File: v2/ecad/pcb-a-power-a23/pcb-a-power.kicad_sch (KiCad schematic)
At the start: 428 parts, among them Q1 2N7002: panel controller high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, Q10 CSD18510Q5B 40 V N-FET, Q11 CSD18510Q5B 40 V N-FET, Q12 CSD18510Q5B 40 V N-FET, Q13 CSD18510Q5B 40 V N-FET, Q14 CSD18510Q5B 40 V N-FET, Q15 CSD18510Q5B 40 V N-FET, Q16 CSD18510Q5B 40 V N-FET, Q17 CSD19532Q5B 100 V N-FET (4.6 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, Q18 CSD19532Q5B 100 V N-FET (4.6 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, Q19 CSD19532Q5B 100 V N-FET (4.6 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, Q2 CSD19532Q5B 100 V N-FET (4.6 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, Q20 CSD19532Q5B 100 V N-FET (4.6 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, Q21 CSD18510Q5B 40 V N-FET, Q22 CSD18510Q5B 40 V N-FET, Q23 CSD18510Q5B 40 V N-FET, Q24 CSD18510Q5B 40 V N-FET, Q25 CSD18510Q5B 40 V N-FET, Q26 CSD18510Q5B 40 V N-FET, Q27 CSD18510Q5B 40 V N-FET (VBUS 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, Q3 CSD19532Q5B 100 V N-FET (4.6 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, Q4 CSD19532Q5B 100 V N-FET (4.6 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, Q5 CSD19532Q5B 100 V N-FET (4.6 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, Q6 2N7002: CHG_INHIBIT high = IL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, Q7 CSD18510Q5B 40 V N-FET, Q8 CSD18510Q5B 40 V N-FET, Q9 CSD18510Q5B 40 V N-FET, U1 LTC2954CTS8-1 push-button on/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, U10 INA226 rail monitor +5V_S3, U11 INA226 rail monitor +5V_DEV, U12 TPS62933DRLR 3 A buck, 3.3 V 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, U13 LM5176PWPR buck-boost control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, U14 INA226 PA rail monitor (0x46), U15 LM5176PWPR buck-boost control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, U16 LM5176PWPR buck-boost control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, U17 INA226 PoE rail monitor (0x47), U18 TPS25740ARGER USB-C PD source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, U19 LM5176PWPR buck-boost control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, U2 LM5176PWPR buck-boost control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, U21 TPS259631DDAR eFuse VBAT -> V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, U22 TPS259631DDAR eFuse VBAT -> V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, U23 TPS259631DDAR eFuse +5V_DEV -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, U26 SN74LVC08APWR quad AND: EMCON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, U27 PCA9555PW (0x21): enables and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, U28 PCA9555PW (0x24): power-good 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, U29 USBLC6-2SC6, U3 BQ25731RSNR 1 to 5 cell buck-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, U4 AP64500SP-13 5 A buck, 5.1 V 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, U5 AP64500SP-13 5 A buck, 5.1 V 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, U6 AP64500SP-13 5 A buck, 5.1 V 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, U7 AP64500SP-13 5 A buck, 5.1 V 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, U8 INA226 rail monitor +5V_S1, U9 INA226 rail monitor +5V_S2

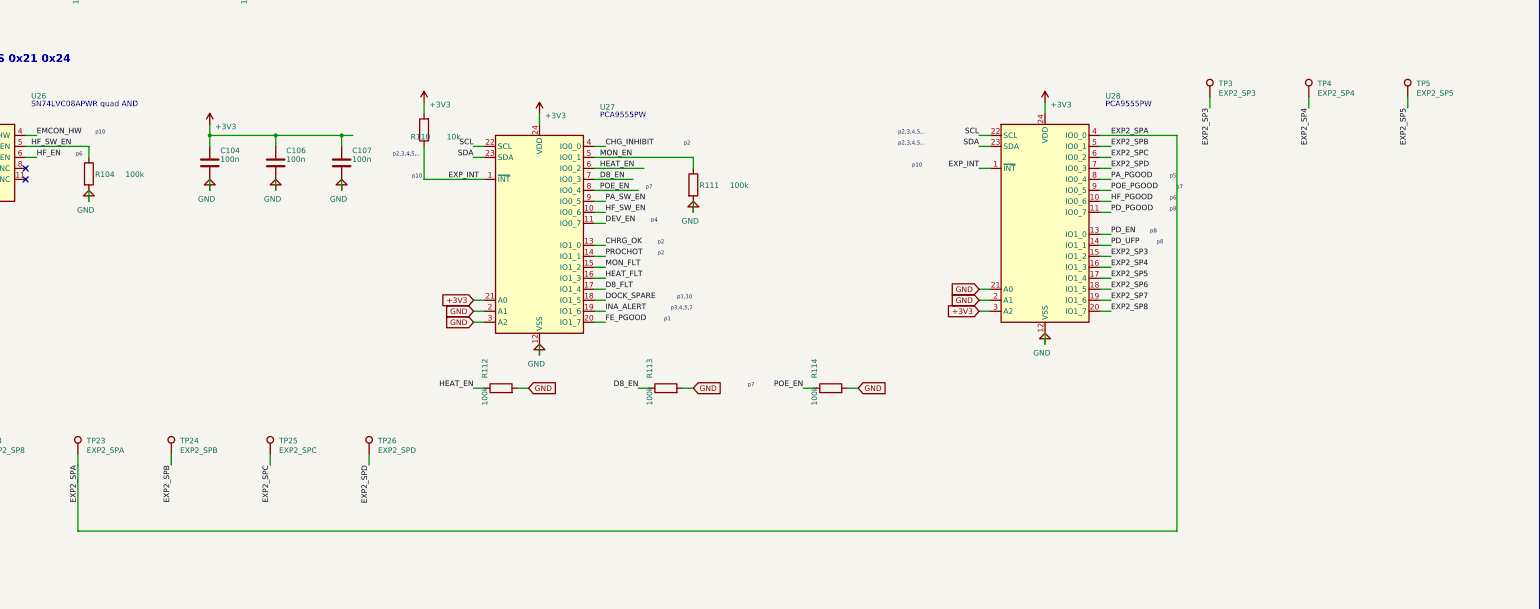
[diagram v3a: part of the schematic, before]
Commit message: fix(pcb-a): four decoupling capacitors were in a region at the other end of the board [MESHSAT-709]
C4, C104, C106 and C107 are named in region CTL at case x 52 to 90 while U1, U26, U27 and U28 are fixed at x -49 to -62, so each sat 109.4, 139.6, 114.6 and 130.7 mm from the pin it decouples. Seats measured on A70's placed board put all four within 1.70 to 1.90 mm with nothing else moved, and the chain proves them at hard 0 with 461 escapes and 2 pads skipped, both the baseline's.

The first arm improved five rows to seven instead of nine, which found the second defect: C106 and C107 are the two expanders' own decoupling and both were declared against U26 pin 14, a part neither serves. With both corrections the chain at HEAD reads 0 moved, 9 already within 3.0 mm, 31 stuck of 40, RESULT ALL PASS and netlist_board 2,148 of 2,148.

The generator edit owes a regeneration: board A's schematic, netlist, sidecar and intent are rebuilt at its own phase and move in this commit. The netlist is identical connection for connection, differing only in its source line, its date and KiCad's own tstamps.
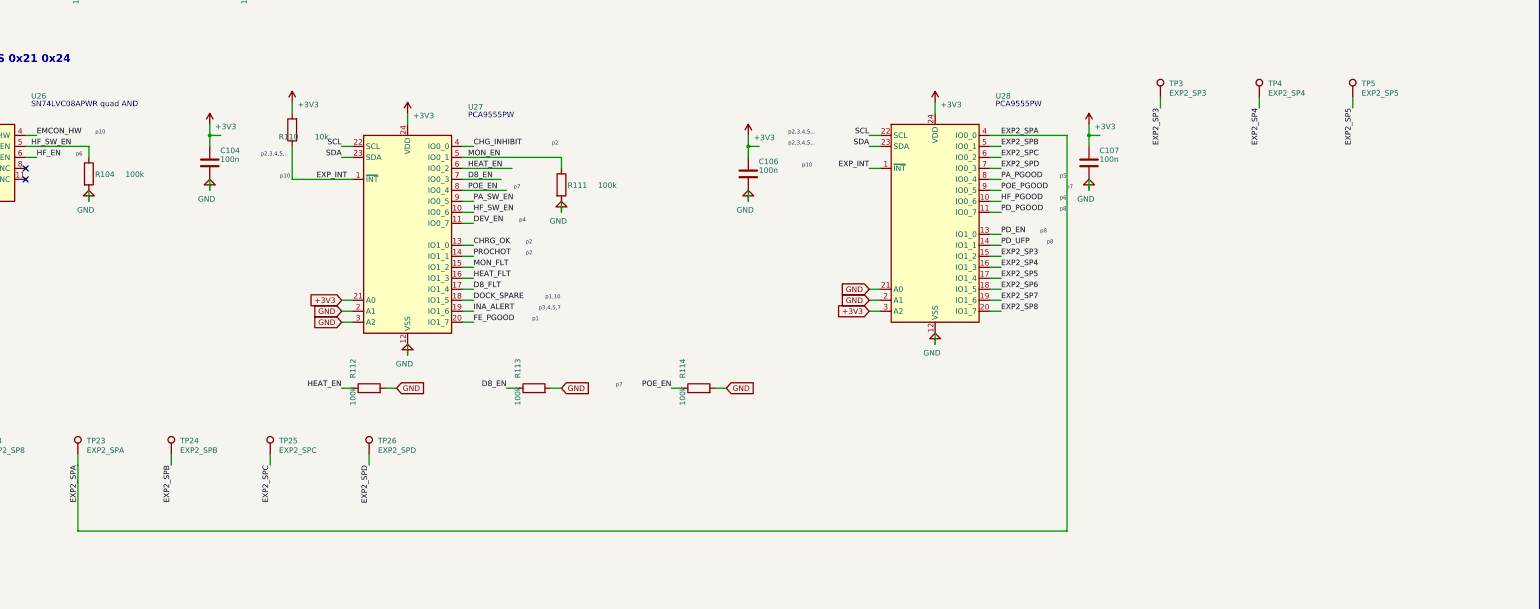
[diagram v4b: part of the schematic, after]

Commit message: fix(v2): boards A, B and D take their round-4 and round-6 circuit corrections, regenerated with parity and every difference traced [MESHSAT-1357]
Review D (parts and circuits) for boards A, B and D. Each board was approved by its reviewer with no blocking item left. This is a prototype design: nothing here has been built or measured, and this commit does not place, route, promote or order any board. Every choice that had more than one option was taken by the session under the owner's standing rule of 26 Sep 2026.

Board A, power and I/O:
- The charger's cell strap now reads 4S (R26 13.3k). The kit sits on the charger's VSYS: the pack reaches VBAT through the blade F1 and the RSR shunt R17 (S-03, S-04).
- Slot rail 2 and the device rail are LM5176 stages with a 7.2 A minimum average limit. The PA rail is limited by its stage's own average current loop (F-PR-04, F-PR-01).
- The heater mat runs from a regulated 12 V buck, U33 (F-PR-06).
- Every LM5176 stage has bootstrap diodes, a slope capacitor, its own loop design and BIAS from VBAT with a bypass. VIN blocking diodes sit on the three stages with external BIAS (R4A-N1, R4A-N2, B2, R4A-N6, R4A-N11).
- The front end has VBUS20 bulk sized for its ripple current, a 4.7 uF soft start sized for board E's vehicle entry, and VISNS behind 2k. A restart guard, U34 (TPS37A010122), holds U2 off until VBUS20 is bled (B3, B4, R4A-N15).
- Power-up: industrial-grade LTC2954, KILL on +3V3, a defined RAIL_EN, PDT set for a four-second override, and resized PI_KILL and PI_SHDN_REQ pulls (S-08).
- A NAND interlock drops the PoE and PD outlets while the PA keys (S-14).
- A low-capacitance ESD array sits on the USB-C CC pins (D-17). The wall data path goes to the Glenair port behind its own eFuse, U32, and the USB-C outlet becomes power only (D-12).

Board B, compute:
- PCIe lanes run from each transmitter to its receiver, with series coupling at the switch. The LimeSDR SuperSpeed pairs run transmitter to receiver. Every used REFCLKO pair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
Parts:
- removed C38, C56: 22u 10V X7R 1210, Capacitor_SMD:C_1210_3225Metric, symbol Device:C
- removed C65, C92: 10u 50V X7R 1210, Capacitor_SMD:C_1210_3225Metric, symbol Device:C
- removed C7: 47n, Capacitor_SMD:C_0603_1608Metric, symbol Device:C
- removed J_PA: 13.8 V to the PA module on the face plate (JST-VH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, Connector_JST:JST_VH_B2P-VH_1x02_P3.96mm_Vertical, symbol Connector_Generic:Conn_01x02
- removed L7: 4.7uH XAL4030-472ME, Inductor_SMD:L_Coilcraft_XAL4030-XXX, symbol Device:L
- removed L8: 6.8uH XAL1010-682ME (Isat 17 A), Inductor_SMD:L_Coilcraft_XAL1010-XXX, symbol Device:L
- removed Q2: CSD19532Q5B 100 V N-FET (4.6 mOhm at VGS 6 V, Pow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, Package_SO:PowerPAK_SO-8_Single, symbol meshsat_ic:Q2
- removed Q23: CSD18510Q5B 40 V N-FET, Package_SO:PowerPAK_SO-8_Single, symbol meshsat_ic:Q23
- removed Q25: CSD18510Q5B 40 V N-FET, Package_SO:PowerPAK_SO-8_Single, symbol meshsat_ic:Q25
- removed R10: 10k, Resistor_SMD:R_0603_1608Metric, symbol Device:R
- removed R31: 5mOhm 1% 2512 (shunt), Resistor_SMD:R_2512_6332Metric, symbol Device:R
- removed R46: 68k (RT: 500 kHz), Resistor_SMD:R_0603_1608Metric, symbol Device:R
- removed R52: 40.2k (300 kHz), Resistor_SMD:R_0603_1608Metric, symbol Device:R
- removed R53, R63, R69, R79, R9: 30k (slope), Resistor_SMD:R_0603_1608Metric, symbol Device:R
- removed R60: 140k 1%, Resistor_SMD:R_0603_1608Metric, symbol Device:R
- removed R72: 10mOhm 1% 2512 (CS), Resistor_SMD:R_2512_6332Metric, symbol Device:R
- removed R90: 750R 1% (ILM: 1.2 A), Resistor_SMD:R_0603_1608Metric, symbol Device:R
- removed U8: INA226 rail monitor +5V_S1, Package_SO:VSSOP-10_3x3mm_P0.5mm, symbol meshsat_ic:U8
- added C10, C137, C144, C46, C9: 100n 25V, Capacitor_SMD:C_0603_1608Metric, symbol Device:C
- added C112: 3.3n, Capacitor_SMD:C_0603_1608Metric, symbol Device:C
- added C129, C130, C134, C138, C141, C145, C146, C191: 1n, Capacitor_SMD:C_0603_1608Metric, symbol Device:C
- added C133, C140, C148, C149, C151: 470p, Capacitor_SMD:C_0603_1608Metric, symbol Device:C
- added C135, C142: 47n, Capacitor_SMD:C_0603_1608Metric, symbol Device:C
- added C136, C143: 4.7u, Capacitor_SMD:C_0805_2012Metric, symbol Device:C
- added C150: 560p, Capacitor_SMD:C_0603_1608Metric, symbol Device:C
- added C152: 680n, Capacitor_SMD:C_0603_1608Metric, symbol Device:C
- added C153, C155, C157, C160, C192, C193, C194, C195, C196, C197, C198, C212, C214, C52: 100n, Capacitor_SMD:C_0603_1608Metric, symbol Device:C
- added C154, C158, C190, C211: 10n, Capacitor_SMD:C_0603_1608Metric, symbol Device:C
- added C156, C161, C162, C51: 22u 25V 1210, Capacitor_SMD:C_1210_3225Metric, symbol Device:C
- added C159: 10u 25V 1210, Capacitor_SMD:C_1210_3225Metric, symbol Device:C
- added C163, C178, C179, C180, C199, C200: 330u 35V Panasonic EEHZK1V331P hybrid polymer (10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, Capacitor_SMD:CP_Elec_10x10, symbol Device:C_Polarized
- added C164, C165, C166, C167, C168, C169, C172, C173: 150u 25V Panasonic EEHZK1E151XP hybrid polymer (7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, Capacitor_SMD:CP_Elec_6.3x7.7, symbol Device:C_Polarized
- added C170, C171, C174, C175: 470u 25V Panasonic EEHZK1E471P hybrid polymer (10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, Capacitor_SMD:CP_Elec_10x10, symbol Device:C_Polarized
- added C176, C177: 10u 100V X7R 1210, Capacitor_SMD:C_1210_3225Metric, symbol Device:C
- added C181, C182, C183, C184, C185, C186, C187, C188, C189, C201, C202, C203, C204, C205, C206: 10u 50V X7R 1210, Capacitor_SMD:C_1210_3225Metric, symbol Device:C
- added C207, C210: 1u 100V 1210, Capacitor_SMD:C_1210_3225Metric, symbol Device:C
- added C208, C209: 1u, Capacitor_SMD:C_0603_1608Metric, symbol Device:C
- added C213: 2.2n, Capacitor_SMD:C_0603_1608Metric, symbol Device:C
- added C87: 1.5n, Capacitor_SMD:C_0603_1608Metric, symbol Device:C
- added D10, D11, D12, D13, D14, D15, D16, D17, D18, D5, D6, D7, D8, D9: BAT46W-7-F Schottky 100V (bootstrap), Diode_SMD:D_SOD-123, symbol Device:D_Schottky
- added D19, D20, D21: BAT46W-7-F Schottky 100V (VIN blocking), Diode_SMD:D_SOD-123, symbol Device:D_Schottky
- added D22: BZT52C12-7-F zener, the restart guard's pull-up c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, Diode_SMD:D_SOD-123, symbol Device:D_Zener
- added D3: SMBJ5.0A, Diode_SMD:D_SMB, symbol Device:D_TVS
- added J_BM9: SMP-MAX slide-on receptacle R222M00720 (underside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, meshsat:Radiall_SMPMAX_R222M00720, symbol Connector:Conn_Coaxial
- added L1: 10uH XAL1010-103ME (Isat 17.5 A), Inductor_SMD:L_Coilcraft_XAL1010-XXX, symbol Device:L
- added L12: 15uH XAL4040-153ME (Isat 2.9 A), Inductor_SMD:L_Coilcraft_XAL4040-XXX, symbol Device:L
- added Q27: CSD18510Q5B 40 V N-FET (VBUS switch), Package_SO:PowerPAK_SO-8_Single, symbol meshsat_ic:Q27
- added Q28: CSD19532Q5B 100 V N-FET (4.6 mOhm at VGS 6 V, Pow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, Package_SO:PowerPAK_SO-8_Single, symbol meshsat_ic:Q28
- added Q29: CSD19532Q5B 100 V N-FET (4.6 mOhm at VGS 6 V, Pow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, Package_SO:PowerPAK_SO-8_Single, symbol meshsat_ic:Q29
- added Q30: CSD19532Q5B 100 V N-FET (4.6 mOhm at VGS 6 V, Pow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, Package_SO:PowerPAK_SO-8_Single, symbol meshsat_ic:Q30
- added Q31: CSD19532Q5B 100 V N-FET (4.6 mOhm at VGS 6 V, Pow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, Package_SO:PowerPAK_SO-8_Single, symbol meshsat_ic:Q31
- added Q32: CSD19532Q5B 100 V N-FET (4.6 mOhm at VGS 6 V, Pow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, Package_SO:PowerPAK_SO-8_Single, symbol meshsat_ic:Q32
- added Q33: CSD19532Q5B 100 V N-FET (4.6 mOhm at VGS 6 V, Pow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, Package_SO:PowerPAK_SO-8_Single, symbol meshsat_ic:Q33
- added Q34: CSD19532Q5B 100 V N-FET (4.6 mOhm at VGS 6 V, Pow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, Package_SO:PowerPAK_SO-8_Single, symbol meshsat_ic:Q34
- added Q35: CSD19532Q5B 100 V N-FET (4.6 mOhm at VGS 6 V, Pow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, Package_SO:PowerPAK_SO-8_Single, symbol meshsat_ic:Q35
- added Q36: 2N7002: FE_RUN high = latch sense held at 0 V (1 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, Package_TO_SOT_SMD:SOT-23, symbol Transistor_FET:2N7002
- added Q37: 2N7002: FE_RUN high = bleed off (1 G, 2 S, 3 D), Package_TO_SOT_SMD:SOT-23, symbol Transistor_FET:2N7002
- added R124: 62k 1%, Resistor_SMD:R_0603_1608Metric, symbol Device:R
- added R135, R172, R179: 100k (MODE: CCM), Resistor_SMD:R_0603_1608Metric, symbol Device:R
- added R142, R187: 10k, Resistor_SMD:R_0603_1608Metric, symbol Device:R
- added R170, R177: 5mOhm 1% 2512 (CS), Resistor_SMD:R_2512_6332Metric, symbol Device:R
- added R173, R180: 100R 1% (CS filter, Kelvin from the shunt's top), Resistor_SMD:R_0603_1608Metric, symbol Device:R
- added R174, R181: 100R 1% (CSG filter, Kelvin from the shunt's grou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, Resistor_SMD:R_0603_1608Metric, symbol Device:R
- added R175, R182: 100R 1% (ISNS+ filter, Kelvin from the shunt's ou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, Resistor_SMD:R_0603_1608Metric, symbol Device:R
- added R176, R183: 100R 1% (ISNS- filter, Kelvin from the shunt's ra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, Resistor_SMD:R_0603_1608Metric, symbol Device:R
- added R178, R193, R197, R198, R201, R206, R4: 100k, Resistor_SMD:R_0603_1608Metric, symbol Device:R
- added R186: 1k 1% (ILM: 0.89 A), Resistor_SMD:R_0603_1608Metric, symbol Device:R
- added R188: 40.2k 1%, Resistor_SMD:R_0603_1608Metric, symbol Device:R
- added R189: 10k 1% (OVLO), Resistor_SMD:R_0603_1608Metric, symbol Device:R
- added R19: 16.5k 1%, Resistor_SMD:R_0603_1608Metric, symbol Device:R
- added R190: 4.7k, Resistor_SMD:R_0603_1608Metric, symbol Device:R
- added R191: 140k 1%, Resistor_SMD:R_0603_1608Metric, symbol Device:R
- added R192: 10k 1%, Resistor_SMD:R_0603_1608Metric, symbol Device:R
- added R194: 20k 1%, Resistor_SMD:R_0603_1608Metric, symbol Device:R
- added R196: 1k, Resistor_SMD:R_0603_1608Metric, symbol Device:R
- added R199: 47k, Resistor_SMD:R_0603_1608Metric, symbol Device:R
- added R200: 33k, Resistor_SMD:R_0603_1608Metric, symbol Device:R
- added R202, R203: 510R 1W 2512 (VBUS20 bleed), Resistor_SMD:R_2512_6332Metric, symbol Device:R
- added R40: 53.6k 1%, Resistor_SMD:R_0603_1608Metric, symbol Device:R
- added R45: 68k (RT: 500 kHz), Resistor_SMD:R_0603_1608Metric, symbol Device:R
- added R6: 240k 1%, Resistor_SMD:R_0603_1608Metric, symbol Device:R
- added R96: 143k 1%, Resistor_SMD:R_0603_1608Metric, symbol Device:R
- added TP21: DOCK_SPARE, TestPoint:TestPoint_Pad_D1.5mm, symbol Connector:TestPoint
- added TP3: EXP2_SP3, TestPoint:TestPoint_Pad_D1.5mm, symbol Connector:TestPoint
- added TP6: EXP2_SP6, TestPoint:TestPoint_Pad_D1.5mm, symbol Connector:TestPoint
- added U12: TPS62933DRLR 3 A buck, 3.3 V logic, Package_TO_SOT_SMD:SOT-583-8, symbol meshsat_ic:U12
- added U17: INA226 PoE rail monitor (0x47), Package_SO:VSSOP-10_3x3mm_P0.5mm, symbol meshsat_ic:U17
- added U19: LM5176PWPR buck-boost controller, PD_VPWR from VB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, Package_SO:HTSSOP-28-1EP_4.4x9.7mm_P0.65mm_EP2.85x5.4mm, symbol meshsat_ic:U19
- added U30: SN74LVC1G00DBVR NAND: OUTLET_OK = NOT (TR_APRS AN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, Package_TO_SOT_SMD:SOT-23-5, symbol meshsat_ic:U30
- added U32: TPS259631DDAR eFuse +5V_DEV -> VBUS_WALL (1k 1% (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, Package_SO:SOIC-8-1EP_3.9x4.9mm_P1.27mm_EP2.29x3mm, symbol meshsat_ic:U32
- added U33: TPS62933DRLR 3 A buck, 12.0 V heater rail, Package_TO_SOT_SMD:SOT-583-8, symbol meshsat_ic:U33
- added U34: TPS37A010122DSKR 65 V OV/UV supervisor: the FE's 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, Package_SON:WSON-10-1EP_2.5x2.5mm_P0.5mm_EP1.2x2mm, symbol meshsat_ic:U34
- C113, C115: value 3.3n -> 100n; LCSC (none) -> C14663
- C139: renamed from U12; value TPS62933DRLR 3 A buck, 3.3 V logic -> 1n; footprint Package_TO_SOT_SMD:SOT-583-8 -> Capacitor_SMD:C_0603_1608Metric; symbol meshsat_ic:U12 -> Device:C; LCSC C3200405 -> (none)
- C147: renamed from C10; value 100n 25V -> 680p; LCSC (none) -> C30816
- C20, C21, C22: value 10u 35V 1210 -> 10u 50V X7R 1210
- C34: value 100n -> 100n 25V
- C35, C36, C47, C48: value 10u 25V 1210 -> 10u 50V X7R 1210
- C37, C39, C49, C50: value 22u 10V X7R 1210 -> 22u 25V 1210; LCSC (none) -> C2918511
- C38: renamed from D3; value SMBJ5.0A -> 22u 25V 1210; footprint Diode_SMD:D_SMB -> Capacitor_SMD:C_1210_3225Metric; symbol Device:D_TVS -> Device:C; LCSC (none) -> C2918511
- C45: renamed from R124; value 62k 1% -> 22u 10V X7R 1210; footprint Resistor_SMD:R_0603_1608Metric -> Capacitor_SMD:C_1210_3225Metric; symbol Device:R -> Device:C
- C5, C86: value 10n -> 220n; LCSC (none) -> C160828
- C56: renamed from U17; value INA226 PoE rail monitor (0x47) -> 22u 10V X7R 1210; footprint Package_SO:VSSOP-10_3x3mm_P0.5mm -> Capacitor_SMD:C_1210_3225Metric; symbol meshsat_ic:U17 -> Device:C; LCSC C49851 -> (none)
- C57, C68, C75: value 10n -> 100n; LCSC (none) -> C14663
- C58: value 100p -> 1.5n; LCSC (none) -> C37788
- C6: value 100p -> 680p; LCSC (none) -> C30816
- C65: renamed from C87; value 100p -> 10u 50V X7R 1210; footprint Capacitor_SMD:C_0603_1608Metric -> Capacitor_SMD:C_1210_3225Metric
- C69: value 100p -> 1n; LCSC (none) -> C1588
- C7: renamed from C9; value 100n 25V -> 4.7u; footprint Capacitor_SMD:C_0603_1608Metric -> Capacitor_SMD:C_0805_2012Metric; LCSC (none) -> C354262
- C76: value 100p -> 470p; LCSC (none) -> C27694
- C92: renamed from J_BM9; value SMP-MAX slide-on receptacle R222M00720 (underside), 5G-DIV to the dock plug -> 10u 50V X7R 1210; footprint meshsat:Radiall_SMPMAX_R222M00720 -> Capacitor_SMD:C_1210_3225Metric; symbol Connector:Conn_Coaxial -> Device:C
- F1: value 25 A mini blade (Keystone 3568 holder): pack node to VBAT -> 25 A mini blade (Keystone 3568 holder): pack node to the RSR shunt
- J_HEAT: value JST-XH 1x2 socket: the heater mat under the 2590 cradle, + and - -> JST-XH 1x2 socket: the pack heater mat (12 V, 7.5 W), fed a regulated 12.0 V: + and -
- J_PA: renamed from R142; value 10k -> 13.8 V to the PA module on the face plate (JST-VH, 16 AWG): + -; footprint Resistor_SMD:R_0603_1608Metric -> Connector_JST:JST_VH_B2P-VH_1x02_P3.96mm_Vertical; symbol Device:R -> Connector_Generic:Conn_01x02; LCSC (none) -> C274411
- J_USBC_OUT: value wall USB-C outlet, power side (pigtail header): VBUS CC1 CC2 GND GND -> wall USB-C outlet, power only (pigtail header): VBUS CC1 CC2 GND GND
- J_USBW: value JST-PH 1x4 socket: the wall USB-C data pair to B16 passes here on the ribbon, this is the pigtail's data side (D+ D- GN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 -> JST-PH 1x4 socket: the Glenair 233-370 USB host feed-through lead (VBUS D- D+ GND), B16 bank 3 hub port 3
- L10: value 22uH XAL1010-223ME (Isat 9 A) -> 15uH XAL1010-153ME (Isat 15.5 A); LCSC (none) -> C2802562
- L3: renamed from C45; value 22u 10V X7R 1210 -> 4.7uH XAL6060-472ME (Isat 11 A); footprint Capacitor_SMD:C_1210_3225Metric -> Inductor_SMD:L_Coilcraft_XAL6060-XXX; symbol Device:C -> Device:L
- L4, L6: value 4.7uH XAL6060-472ME (Isat 11 A) -> 6.8uH XAL1010-682ME (Isat 21.8 A); footprint Inductor_SMD:L_Coilcraft_XAL6060-XXX -> Inductor_SMD:L_Coilcraft_XAL1010-XXX
- L7: renamed from Q18; value CSD19532Q5B 100 V N-FET (4.6 mOhm at VGS 6 V, PowerPAK SO-8 / SON-8 5x6) -> 4.7uH XAL4030-472ME; footprint Package_SO:PowerPAK_SO-8_Single -> Inductor_SMD:L_Coilcraft_XAL4030-XXX; symbol meshsat_ic:Q18 -> Device:L; LCSC C473333 -> (none)
- L8: renamed from R135; value 100k (MODE: CCM) -> 6.8uH XAL1010-682ME (Isat 21.8 A); footprint Resistor_SMD:R_0603_1608Metric -> Inductor_SMD:L_Coilcraft_XAL1010-XXX; symbol Device:R -> Device:L
- Q18: renamed from TP3; value EXP2_SP3 -> CSD19532Q5B 100 V N-FET (4.6 mOhm at VGS 6 V, PowerPAK SO-8 / SON-8 5x6); footprint TestPoint:TestPoint_Pad_D1.5mm -> Package_SO:PowerPAK_SO-8_Single; symbol Connector:TestPoint -> meshsat_ic:Q18; LCSC (none) -> C473333; now in the parts list
- Q2: renamed from R19; value 16.5k 1% -> CSD19532Q5B 100 V N-FET (4.6 mOhm at VGS 6 V, PowerPAK SO-8 / SON-8 5x6); footprint Resistor_SMD:R_0603_1608Metric -> Package_SO:PowerPAK_SO-8_Single; symbol Device:R -> meshsat_ic:Q2; LCSC (none) -> C473333
- Q23: renamed from R96; value 100k 1% -> CSD18510Q5B 40 V N-FET; footprint Resistor_SMD:R_0603_1608Metric -> Package_SO:PowerPAK_SO-8_Single; symbol Device:R -> meshsat_ic:Q23
- Q25: renamed from TP21; value DOCK_SPARE -> CSD18510Q5B 40 V N-FET; footprint TestPoint:TestPoint_Pad_D1.5mm -> Package_SO:PowerPAK_SO-8_Single; symbol Connector:TestPoint -> meshsat_ic:Q25; now in the parts list
- Q38: renamed from R45; value 68k (RT: 500 kHz) -> CSD19532Q5B 100 V N-FET (the VBUS20 bleed switch); footprint Resistor_SMD:R_0603_1608Metric -> Package_SO:PowerPAK_SO-8_Single; symbol Device:R -> meshsat_ic:Q38; LCSC (none) -> C473333
- R10: renamed from L1; value 10uH XAL1010-103ME (Isat 14 A) -> 15k; footprint Inductor_SMD:L_Coilcraft_XAL1010-XXX -> Resistor_SMD:R_0603_1608Metric; symbol Device:L -> Device:R; LCSC (none) -> C22809
- R100: value 100k 1% -> 40.2k 1%; LCSC (none) -> C12447
- R103, R104, R111, R112, R113, R114, R143, R21: value 100k -> 4.7k
- R115: value 68k (RT: 500 kHz) -> 40.2k (206 kHz)
- R130, R132: value 22k -> 2.2k; LCSC (none) -> C4190
- R14: value 62k 1% -> 91k 1%; LCSC (none) -> C23265
- R15: LCSC (none) -> C25804
- R171: renamed from C52; value 100n -> 100k; footprint Capacitor_SMD:C_0603_1608Metric -> Resistor_SMD:R_0603_1608Metric; symbol Device:C -> Device:R
- R184: renamed from R4; value 100k -> 39k 1%; LCSC (none) -> C23153
- R195: renamed from R6; value 240k 1% -> 2k; LCSC (none) -> C22975
- R204: renamed from C112; value 3.3n -> 510R 1W 2512 (VBUS20 bleed); footprint Capacitor_SMD:C_0603_1608Metric -> Resistor_SMD:R_2512_6332Metric; symbol Device:C -> Device:R; LCSC (none) -> C36171
- R205: renamed from L3; value 4.7uH XAL6060-472ME (Isat 11 A) -> 510R 1W 2512 (VBUS20 bleed); footprint Inductor_SMD:L_Coilcraft_XAL6060-XXX -> Resistor_SMD:R_2512_6332Metric; symbol Device:L -> Device:R; LCSC (none) -> C36171
- R26: value 60.4k 1% (CELL_BATPRESZ: 4S per Table, from VDDA) -> 13.3k 1% (CELL_BATPRESZ: 4S, 75 percent of VDDA); LCSC (none) -> C25952
- R3: value 100k -> 10k
- R31: renamed from R40; value 53.6k 1% -> 5mOhm 1% 2512 (shunt); footprint Resistor_SMD:R_0603_1608Metric -> Resistor_SMD:R_2512_6332Metric
- R35, R43: value 5mOhm 1% 2512 (shunt) -> 6mOhm 1% 2512 (ISNS); LCSC (none) -> C843882
- R46: renamed from C51; value 22u 10V X7R 1210 -> 40.2k (206 kHz); footprint Capacitor_SMD:C_1210_3225Metric -> Resistor_SMD:R_0603_1608Metric; symbol Device:C -> Device:R
- R5: value 100k -> 1k
- R52: renamed from U19; value LM5176PWPR buck-boost controller, PD_VPWR from VBAT -> 40.2k (206 kHz); footprint Package_SO:HTSSOP-28-1EP_4.4x9.7mm_P0.65mm_EP2.85x5.4mm -> Resistor_SMD:R_0603_1608Metric; symbol meshsat_ic:U19 -> Device:R; LCSC C442493 -> (none)
- R54: value 10k -> 6.8k; LCSC (none) -> C23212
- R55: value 2mOhm 1% 2512 (ISNS) -> 6mOhm 1% 2512 (ISNS); LCSC (none) -> C843882
- R60: renamed from Q27; value CSD18510Q5B 40 V N-FET (VBUS switch) -> 140k 1%; footprint Package_SO:PowerPAK_SO-8_Single -> Resistor_SMD:R_0603_1608Metric; symbol meshsat_ic:Q27 -> Device:R
- R62, R68, R78, R8: value 40.2k (300 kHz) -> 40.2k (206 kHz)
- R64, R80: value 10k -> 3.3k; LCSC (none) -> C22978
- R70: value 10k -> 4.7k; LCSC (none) -> C23162
- R72: renamed from TP6; value EXP2_SP6 -> 10mOhm 1% 2512 (CS); footprint TestPoint:TestPoint_Pad_D1.5mm -> Resistor_SMD:R_2512_6332Metric; symbol Connector:TestPoint -> Device:R; now in the parts list
- R90: renamed from C130; value 1n -> 750R 1% (ILM: 1.2 A); footprint Capacitor_SMD:C_0603_1608Metric -> Resistor_SMD:R_0603_1608Metric; symbol Device:C -> Device:R
- R92: value 100k 1% -> 143k 1%; LCSC (none) -> C22877
- TP23: value EXP2_SPA -> USBX_EN
- TP24: value EXP2_SPB -> USBX_FLT
- U1: value LTC2954CTS8-1 push-button on/off controller -> LTC2954ITS8-1 push-button on/off controller, -40 to 85 C; LCSC C683782 -> C580654
- U22: value TPS259631DDAR eFuse VBAT -> VHEAT (909R 1% (ILM: 1.0 A)) -> TPS259631DDAR eFuse VBAT -> VHEAT_IN (909R 1% (ILM: 1.0 A))
- U26: value SN74LVC08APWR quad AND: EMCON gates for the PA rail, the HF rail and the D8 inhibit -> SN74LVC08APWR quad AND: EMCON gates for the PA and HF rails, the outlet interlock for PoE and USB-C
- U31: renamed from C129; value 1n -> TPD2E2U06QDBZRQ1 low-capacitance ESD array, USB-C CC1 and CC2 at the connector; footprint Capacitor_SMD:C_0603_1608Metric -> Package_TO_SOT_SMD:SOT-23; symbol Device:C -> meshsat_ic:U31; LCSC (none) -> C488151
- U5: value AP64500SP-13 5 A buck, 5.1 V rail +5V_S2 -> LM5176PWPR buck-boost controller, +5V_S2 from VBAT; footprint Package_SO:SOIC-8-1EP_3.9x4.9mm_P1.27mm_EP2.29x3mm -> Package_SO:HTSSOP-28-1EP_4.4x9.7mm_P0.65mm_EP2.85x5.4mm; LCSC C2070920 -> C442493
- U7: value AP64500SP-13 5 A buck, 5.1 V rail +5V_DEV -> LM5176PWPR buck-boost controller, +5V_DEV from VBAT; footprint Package_SO:SOIC-8-1EP_3.9x4.9mm_P1.27mm_EP2.29x3mm -> Package_SO:HTSSOP-28-1EP_4.4x9.7mm_P0.65mm_EP2.85x5.4mm; LCSC C2070920 -> C442493
- U8: renamed from C46; value 100n -> INA226 rail monitor +5V_S1; footprint Capacitor_SMD:C_0603_1608Metric -> Package_SO:VSSOP-10_3x3mm_P0.5mm; symbol Device:C -> meshsat_ic:U8; LCSC (none) -> C49851
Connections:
- net CH_SRP is gone; now on net VBAT: C23.1, C24.1, C25.1, Q10.5 (VBAT), R149.1, R17.1, U3.22 (VBAT)
- net +12V_HF: now also R60.1, C172.1, C173.1, C196.1
- net +13V8_PA: now also C65.1, J_PA.1 (Pin_1), C170.1, C171.1, C195.1
- net +3V3: now also L7.2, R171.2, R42.2, U8.6 (+3V3), C153.1, D3.1 (A1), R142.2, R178.2, R187.2, R4.2, U17.1 (+3V3), U17.6 (+3V3)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; no longer C38.1 (A1), C56.6 (+3V3), J_PA.2
- net +54V_POE: now also C176.1, C177.1, U17.9 (+54V_POE); no longer C56.9 (+54V_POE)
- net +5V_DEV: now also U7.12 (+5V_DEV), C155.1, C167.1, C168.1, C169.1, C51.1, R183.1, R188.1, R40.1, U32.4 (+5V_DEV); no longer R31.1, R46.1, U29.5 (VBUS)
- net +5V_S1: now also R31.2, U8.8 (+5V_S1), U8.9 (+5V_S1)
- net +5V_S2: now also C38.1, U5.12 (+5V_S2), C164.1, C165.1, C166.1, R176.1
- net +5V_S3: now also C45.1; no longer L3.1
- net B33_BST: now also C52.1, U12.6 (B33_BST); no longer C139.6 (B33_BST), R171.1
- net B33_FB: now also U12.8 (B33_FB); no longer C139.8 (B33_FB)
- net B33_SS: now also U12.7 (B33_SS); no longer C139.7 (B33_SS)
- net B33_SW: now also L7.1, C52.2, U12.5 (B33_SW); no longer C139.5 (B33_SW), R171.2
- net CELL+: no longer R148.1, R17.2
- net CHG_ILIM: now also R19.2; no longer Q2.2
- net CH_ACN: now also C190.1, C191.1; no longer C20.1, C21.1, C22.1
- net DEV_EN: now also U7.1 (DEV_EN); no longer U7.3 (DEV_EN)
- net DOCK_SPARE: now also TP21.1; no longer Q25.1
- net EXP2_SP3: now also TP3.1; no longer Q18.1
- net EXP2_SP6: now also TP6.1; no longer R72.1
- net FE_BOOT1: now also C9.1, D9.1 (K); no longer C7.1
- net FE_BOOT2: now also C10.1, D10.1 (K); no longer C147.1
- net FE_COMP: now also R10.1
- net FE_COMPC: now also R10.2
- net FE_EN: now also C213.1, R199.2, R206.1; no longer R14.2, R15.1
- net FE_FB: now also R6.2; no longer R195.2
- net FE_HDRV1: now also Q2.4 (FE_HDRV1)
- net FE_OUT: now also C13.1, C14.1, C15.1
- net FE_SLOPE: now also C147.1
- net FE_SS: now also C7.1
- net FE_SW1: now also Q2.1 (FE_SW1), Q2.2 (FE_SW1), Q2.3 (FE_SW1), C9.2, L1.1; no longer C7.2, R10.1
- net FE_SW2: now also C10.2, L1.2; no longer C147.2, R10.2
- net FE_VCC: now also D10.2 (A), D9.2 (A)
- net GND: now also C147.2, C45.2, C56.2, C7.2, J_PA.2 (Pin_2), Q38.1 (GND), Q38.3 (GND), R184.2, R52.2, R72.2, R90.2, U31.3 (GND)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; no longer C139.4 (GND), C56.7 (GND), J_USBW.3 (Pin_3), L3.2, R204.2, R42.2, R52.10 (GND), R52.22 (GND), R52.29 (GND), R52.5 (GND), U26.10 (GND), U26.12 (GND)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
- net HF_BOOT1: now also D13.1 (K)
- net HF_BOOT2: now also D14.1 (K)
- net HF_CS: now also Q23.1 (HF_CS), Q23.2 (HF_CS), Q23.3 (HF_CS)
- net HF_EN: now also R124.1, R124.2; no longer C45.1, C45.2
- net HF_FB: now also R60.2
- net HF_ISNS_N: now also C130.2; no longer R90.2
- net HF_ISNS_P: now also C130.1; no longer R90.1
- net HF_LDRV2: now also Q23.4 (HF_LDRV2)
- net HF_SLOPE: now also C149.1
- net HF_SW2: now also Q23.5 (HF_SW2)
- net HF_VCC: now also D13.2 (A), D14.2 (A)
- net EXP2_SPA renamed USBX_EN
- net EXP2_SPB renamed USBX_FLT
- net S2_BOOT renamed S2_BOOT1
- net S2_SW renamed S2_SW1
- removed net SD_BOOT: U7.1 (SD_BOOT), U8.1
- removed net SD_SW: L6.1, U7.8 (SD_SW), U8.2
- new net CELL_FUSED: C1.1, C2.1, C3.1, F1.2, R148.1, R17.2
- new net FE_BLEED: Q38.5 (FE_BLEED), R202.2, R203.2, R204.2, R205.2
- new net FE_BLEED_G: Q37.3 (D), Q38.4 (FE_BLEED_G), R201.2
- new net FE_CTR2: C212.1, U34.9 (FE_CTR2)
- new net FE_GVDD: C210.1, R196.2, U34.1 (FE_GVDD)
- new net FE_LATCH: Q36.3 (D), R197.2, U34.2 (FE_LATCH)
- new net FE_RUN: Q36.1 (G), Q37.1 (G), R198.2, R199.1, U34.4 (FE_RUN), U34.5 (FE_RUN)
- new net FE_UVS: C211.1, R14.2, R15.1, U34.3 (FE_UVS)
- new net FE_VINP: C207.1, D19.1 (K), U2.2 (FE_VINP)
- new net FE_VISNS: R195.2, U2.3 (FE_VISNS)
- new net FE_VZ: C214.1, D22.1 (K), R198.1, R200.2, R201.1
- new net HF_VINP: C209.1, D21.1 (K), U15.2 (HF_VINP)
- new net HT_BST: C157.1, U33.6 (HT_BST)
- new net HT_EN: R193.2, R194.1, U33.2 (HT_EN)
- new net HT_FB: R191.2, R192.1, U33.8 (HT_FB)
- new net HT_SS: C158.1, U33.7 (HT_SS)
- new net HT_SW: C157.2, L12.1, U33.5 (HT_SW)
- new net OUTLET_OK: U26.10 (OUTLET_OK), U26.13 (OUTLET_OK), U30.4 (OUTLET_OK)
- new net PA_VINP: C208.1, D20.1 (K), U13.2 (PA_VINP)
- new net PD_SW_EN: R143.1, U26.12 (PD_SW_EN), U28.13 (IO1_0)
- new net POE_SW_EN: R114.1, U26.9 (POE_SW_EN), U27.8 (IO0_4)
- new net S2_BOOT2: C137.1, D6.1 (K), U5.20 (S2_BOOT2)
- new net S2_CS: Q29.1 (S2_CS), Q29.2 (S2_CS), Q29.3 (S2_CS), Q30.1 (S2_CS), Q30.2 (S2_CS), Q30.3 (S2_CS), R170.1, R173.1
- new net S2_CSF: C138.1, R173.2, U5.16 (S2_CSF)
- new net S2_CSGF: C138.2, R174.2, U5.15 (S2_CSGF)
- new net S2_HDRV1: Q28.4 (S2_HDRV1), U5.27 (S2_HDRV1)
- new net S2_HDRV2: Q31.4 (S2_HDRV2), U5.19 (S2_HDRV2)
- new net S2_ISNS_N: C139.2, R176.2, U5.13 (S2_ISNS_N)
- new net S2_LDRV1: Q29.4 (S2_LDRV1), U5.25 (S2_LDRV1)
- new net S2_LDRV2: Q30.4 (S2_LDRV2), U5.21 (S2_LDRV2)
- new net S2_MODE: R172.1, U5.4 (S2_MODE)
- new net S2_PGOOD: R171.1, U5.17 (S2_PGOOD)
- new net S2_SLOPE: C133.1, U5.7 (S2_SLOPE)
- new net S2_SS: C135.1, U5.8 (S2_SS)
- new net S2_SW2: C137.2, L4.2, Q30.5 (S2_SW2), Q31.1 (S2_SW2), Q31.2 (S2_SW2), Q31.3 (S2_SW2), U5.18 (S2_SW2)
- new net S2_VCC: C136.1, D5.2 (A), D6.2 (A), R172.2, U5.23 (S2_VCC)
- new net SD_BOOT1: C46.1, D7.1 (K), U7.26 (SD_BOOT1)
- new net SD_BOOT2: C144.1, D8.1 (K), U7.20 (SD_BOOT2)
- new net SD_CS: Q33.1 (SD_CS), Q33.2 (SD_CS), Q33.3 (SD_CS), Q34.1 (SD_CS), Q34.2 (SD_CS), Q34.3 (SD_CS), R177.1, R180.1
- new net SD_CSF: C145.1, R180.2, U7.16 (SD_CSF)
- new net SD_CSGF: C145.2, R181.2, U7.15 (SD_CSGF)
- new net SD_HDRV1: Q32.4 (SD_HDRV1), U7.27 (SD_HDRV1)
- new net SD_HDRV2: Q35.4 (SD_HDRV2), U7.19 (SD_HDRV2)
- new net SD_ISNS_N: C146.2, R183.2, U7.13 (SD_ISNS_N)
- new net SD_ISNS_P: C146.1, R182.2, U7.14 (SD_ISNS_P)
- new net SD_LDRV1: Q33.4 (SD_LDRV1), U7.25 (SD_LDRV1)
- new net SD_LDRV2: Q34.4 (SD_LDRV2), U7.21 (SD_LDRV2)
- new net SD_MODE: R179.1, U7.4 (SD_MODE)
- new net SD_PGOOD: R178.1, U7.17 (SD_PGOOD)
- new net SD_SLOPE: C140.1, U7.7 (SD_SLOPE)
- new net SD_SS: C142.1, U7.8 (SD_SS)
- new net SD_SW1: C46.2, L6.1, Q32.1 (SD_SW1), Q32.2 (SD_SW1), Q32.3 (SD_SW1), Q33.5 (SD_SW1), U7.28 (SD_SW1)
- new net SD_SW2: C144.2, L6.2, Q34.5 (SD_SW2), Q35.1 (SD_SW2), Q35.2 (SD_SW2), Q35.3 (SD_SW2), U7.18 (SD_SW2)
- new net SD_VCC: C143.1, D7.2 (A), D8.2 (A), R179.2, U7.23 (SD_VCC)
- new net U32_DVDT: C154.1, U32.2 (U32_DVDT)
- new net U32_ILM: R186.1, U32.7 (U32_ILM)
- new net U32_OVLO: R188.2, R189.1, U32.8 (U32_OVLO)
- new net VBUS_WALL: C156.1, J_USBW.1 (Pin_1), U29.5 (VBUS), U32.5 (VBUS_WALL)
- new net VHEAT_IN: C159.1, C160.1, R193.1, U22.5 (VHEAT_IN), U33.3 (VHEAT_IN)
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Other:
- note added: "13.3k 1%"
- note added: "150u 25V"
- note added: "15uH XAL1010-153ME"
- note added: "15uH XAL4040-153ME"
- note added: "1k 1%"
- note added: "1u 100V"
- note added: "22u 25V"
- note added: "3.3 V LOGIC | PA RAIL"
- note added: "330u 35V"
- note added: "470u 25V"
- note added: "470u 25V Panasonic EEHZK1E471P hyb.."
- note added: "510R 1W"
- note added: "6mOhm 1%"
- note added: "BAT46W-7-F Schottky 100V"
- note added: "BZT52C12-7-F zener"
- note added: "CHARGER BQ25731: 4S FROM THE 20 V BUS, SYSTEM ON VSYS (VBAT), PACK BEYOND RSR, I2C 0x6B"
- note added: "DEVICE RAIL"
- note added: "DEVICE RAIL: LM5176 5.1 V (7.2 A MINIMUM LIMIT) + INA226 0x45"
- note added: "EFUSES | EMCON GATES 74LVC08, OUTLET INTERLOCK, EXPANDERS 0x21 0x24"
- note added: "EFUSES: MONITOR, HEATER (12.0 V BUCK), D8 5 V"
- note added: "EFUSES: MONITOR, HEATER (12.0 V BUCK), D8 5 V (continued)"
- note added: "ELEVEN BLIND-MATE RF SITES | TEST POINTS, FLAGS | OTHER PARTS (not in a section list)"
- note added: "ELEVEN BLIND-MATE RF SITES: SMA JACK (TOP) + SMP-MAX RECEPTACLE (UNDERSIDE) (continued)"
- note added: "EMCON GATES 74LVC08, OUTLET INTERLOCK, EXPANDERS 0x21 0x24"
- note added: "FRONT END"
- note added: "LTC2954ITS8-1 push-button on/off c.."
- note added: "PA RAIL | HF RAIL"
- note added: "PA RAIL: LM5176 13.8 V 6 A, EMCON GATED, INA226 0x46 (continued)"
- note added: "RIBBON J_AB1 2x13, WALL-PORT RIBBON J_AB2 2x5, MEZZANINE HARNESS J_MEZZ1 2x8, GLENAIR WALL USB HOST PORT"
- note added: "RIBBON J_AB1 2x13, WALL-PORT RIBBON J_AB2 2x5, MEZZANINE HARNESS J_MEZZ1 2x8, GLENAIR WALL USB HOST PORT | ELEVEN BLIND-MATE RF SITES"
- note added: "SLOT RAIL S2 | SLOT RAIL S3"
- note added: "SLOT RAIL S2: LM5176 5.1 V (7.2 A MINIMUM LIMIT) + INA226 0x41"
- note added: "SLOT RAIL S2: LM5176 5.1 V (7.2 A MINIMUM LIMIT) + INA226 0x41 (continued)"
- note added: "SN74LVC1G00DBVR NAND"
- note added: "TPD2E2U06QDBZRQ1 low-capacitance E.."
- note added: "TPS259631DDAR eFuse +5V_DEV -> VBU.."
- note added: "TPS259631DDAR eFuse VBAT -> VHEAT_IN"
- note added: "TPS37A010122DSKR 65 V OV/UV superv.."
- note added: "USB-C PD OUTLET | EFUSES"
- note added: "USB-C PD OUTLET: TPS25740A + LM5176 5/9/15 V STAGE (continued)"
- note added: "decoupling of U19"
- note added: "decoupling of U7"
- note added: "p1,12"
- note added: "p1,14"
- note added: "p1,7"
- note added: "p10,14"
- note added: "p11,14"
- note added: "p12"
- note added: "p12,13"
- note added: "p12,14"
- note added: "p13"
- note added: "p13,14"
- note added: "p14"
- note added: "p3,4,5,6,.."
- note added: "p3,4,5,8,.."
- note added: "p3,4,6,8,.."
- note added: "p3,5,6,8,.."
- note added: "p4,5,6,8,.."
- note added: "p4,5,8,9,.."
- note added: "p4,6,8,9,.."
- note added: "p5,6,8,9,.."
- note added: "p7,12"
- note added: "p7,13"
- note added: "p7,14"
- note added: "p7,8"
- note added: "p8,14"
- note added: "page 1 of 14 MeshSat field kit V2, CERN-OHL-S-2.0 PROTOTYPE, nothing built 2026-09-26"
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
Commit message: fix(v2): boards A and B draw their ten one-way clamps with a cathode pin, and all six boards are regenerated with parity [MESHSAT-1357]
The ten unidirectional suppressors of boards A and B were drawn on KiCad's Device:D_TVS. That is the bidirectional
symbol, and its pins A1/A2 name no cathode, so TRN-001 read FAIL on both boards (A: 4 symbol mismatches, B: 6). Each
part was already the right way round, with pad 1, the banded cathode, on its conductor.

They now go through kisch.tvs(), as boards D and P already do. The direction is read from the part number
(kisch.tvs_direction), the protected conductor and its return are named, and the call is recorded in the board's
intent under "clamps":
  A: D1 SMCJ18A VBAT, D2 SMCJ40A VIN_RAW, D3 SMBJ5.0A +3V3, D4 SMBJ18A PD_VBUS
  B: D1 SMBJ5.0A +5V_DEV, D2 SMBJ58A +54V_POE, D101/D201/D301 SMBJ6.0A +5V_S1..S3, D520 SMBJ5.0A +3V3_M2C2
Each call replaces its own line, so no line number moves in either generator.

kisch.py's comments now cite the Littelfuse SMBJ, Diodes DS19002, MDD SMBJ and Nexperia PESD12VL1BA sheets at their
filed v2/vendor paths, each sha256 read off the filed bytes and equal to v2/vendor/SOURCES.yaml. They cite DS18004
at v2/vendor/diodes/diodes-bzt52c-ds18004.pdf, and they correct the stale line saying board E's D3 had no code.

kisch.py is in every board's generator identity, so boards A, B, C, D, E and P were regenerated on the KiCad box
(9.0.9), next to main's own generators:
- main's generators against main's committed files: PARITY or PARITY_AFTER_NOISE on all 36 artefacts;
- an independent comparison (every part record, every net's nodes with pin, pinfunction and pintype, libparts,
  intents, schematic bodies) finds 0 unexpected differences. A and B change only the ten clamps: libsource
  D_TVS to D_Zener, pin names A1/A2 to K/A on the same nets, and the intent gains clamps. ERC changes only the
  symbol name in the ten lib_symbol_issues warnings. BOMs are at parity. C, D, E and P change only their sid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
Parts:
- D1, D2, D3, D4: symbol Device:D_TVS -> Device:D_Zener
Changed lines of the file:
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@@
 	(wire (pts (xy 265.43 29.21) (xy 262.89 29.21)) (stroke (width 0) (type default)))
 	(wire (pts (xy 273.05 29.21) (xy 275.59 29.21)) (stroke (width 0) (type default)))
-	(symbol (lib_id "Device:D_TVS") (at 311.15 27.94 0) (unit 1) (exclude_from_sim no) (in_bom yes) (on_board yes) (dnp no)
+	(symbol (lib_id "Device:D_Zener") (at 311.15 27.94 0) (unit 1) (exclude_from_sim no) (in_bom yes) (on_board yes) (dnp no)
 		(property "Reference" "D1" (at 309.64 25.40 0) (effects (font (size 1.27 1.27)) (justify left bottom)))
 		(property "Value" "SMCJ18A (VBAT clamp)" (at 305.88 32.19 0) (effects (font (size 1.27 1.27)) (justify left bottom) (hide yes)))
@@
 		(instances (project "pcb-a-power" (path "/5663fbcf-143d-5acc-8e65-3ad892df2ec3" (reference "#PWR035") (unit 1))))
 	)
-	(symbol (lib_id "Device:D_TVS") (at 744.22 49.53 270) (unit 1) (exclude_from_sim no) (in_bom yes) (on_board yes) (dnp no)
+	(symbol (lib_id "Device:D_Zener") (at 744.22 49.53 270) (unit 1) (exclude_from_sim no) (in_bom yes) (on_board yes) (dnp no)
 		(property "Reference" "D2" (at 745.89 47.43 0) (effects (font (size 1.27 1.27)) (justify left bottom)))
 		(property "Value" "SMCJ40A (VIN_RAW clamp behind E6's filter: 40 V standoff on a line specified to 36)" (at 745.89 49.45 0) (effects (font (size 1.27 1.27)) (justify left bottom) (hide yes)))
@@
 	(wire (pts (xy 1043.94 326.39) (xy 1041.40 326.39)) (stroke (width 0) (type default)))
 	(wire (pts (xy 1051.56 326.39) (xy 1054.10 326.39)) (stroke (width 0) (type default)))
-	(symbol (lib_id "Device:D_TVS") (at 1092.20 325.12 0) (unit 1) (exclude_from_sim no) (in_bom yes) (on_board yes) (dnp no)
+	(symbol (lib_id "Device:D_Zener") (at 1092.20 325.12 0) (unit 1) (exclude_from_sim no) (in_bom yes) (on_board yes) (dnp no)
 		(property "Reference" "D3" (at 1090.69 322.58 0) (effects (font (size 1.27 1.27)) (justify left bottom)))
 		(property "Value" "SMBJ5.0A" (at 1086.17 329.37 0) (effects (font (size 1.27 1.27)) (justify left bottom)))
@@
 		(property "Intersheetrefs" "${INTERSHEET_REFS}" (at 875.03 698.50 0) (effects (font (size 1.27 1.27)) (hide yes)))
 	)
-	(symbol (lib_id "Device:D_TVS") (at 909.32 698.50 0) (unit 1) (exclude_from_sim no) (in_bom yes) (on_board yes) (dnp no)
+	(symbol (lib_id "Device:D_Zener") (at 909.32 698.50 0) (unit 1) (exclude_from_sim no) (in_bom yes) (on_board yes) (dnp no)
 		(property "Reference" "D4" (at 907.81 695.96 0) (effects (font (size 1.27 1.27)) (justify left bottom)))
 		(property "Value" "SMBJ18A (VBUS clamp at the outlet)" (at 904.05 702.75 0) (effects (font (size 1.27 1.27)) (justify left bottom) (hide yes)))
